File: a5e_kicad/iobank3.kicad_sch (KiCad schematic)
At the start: 3 parts, among them U7 A5EB013B-B23B

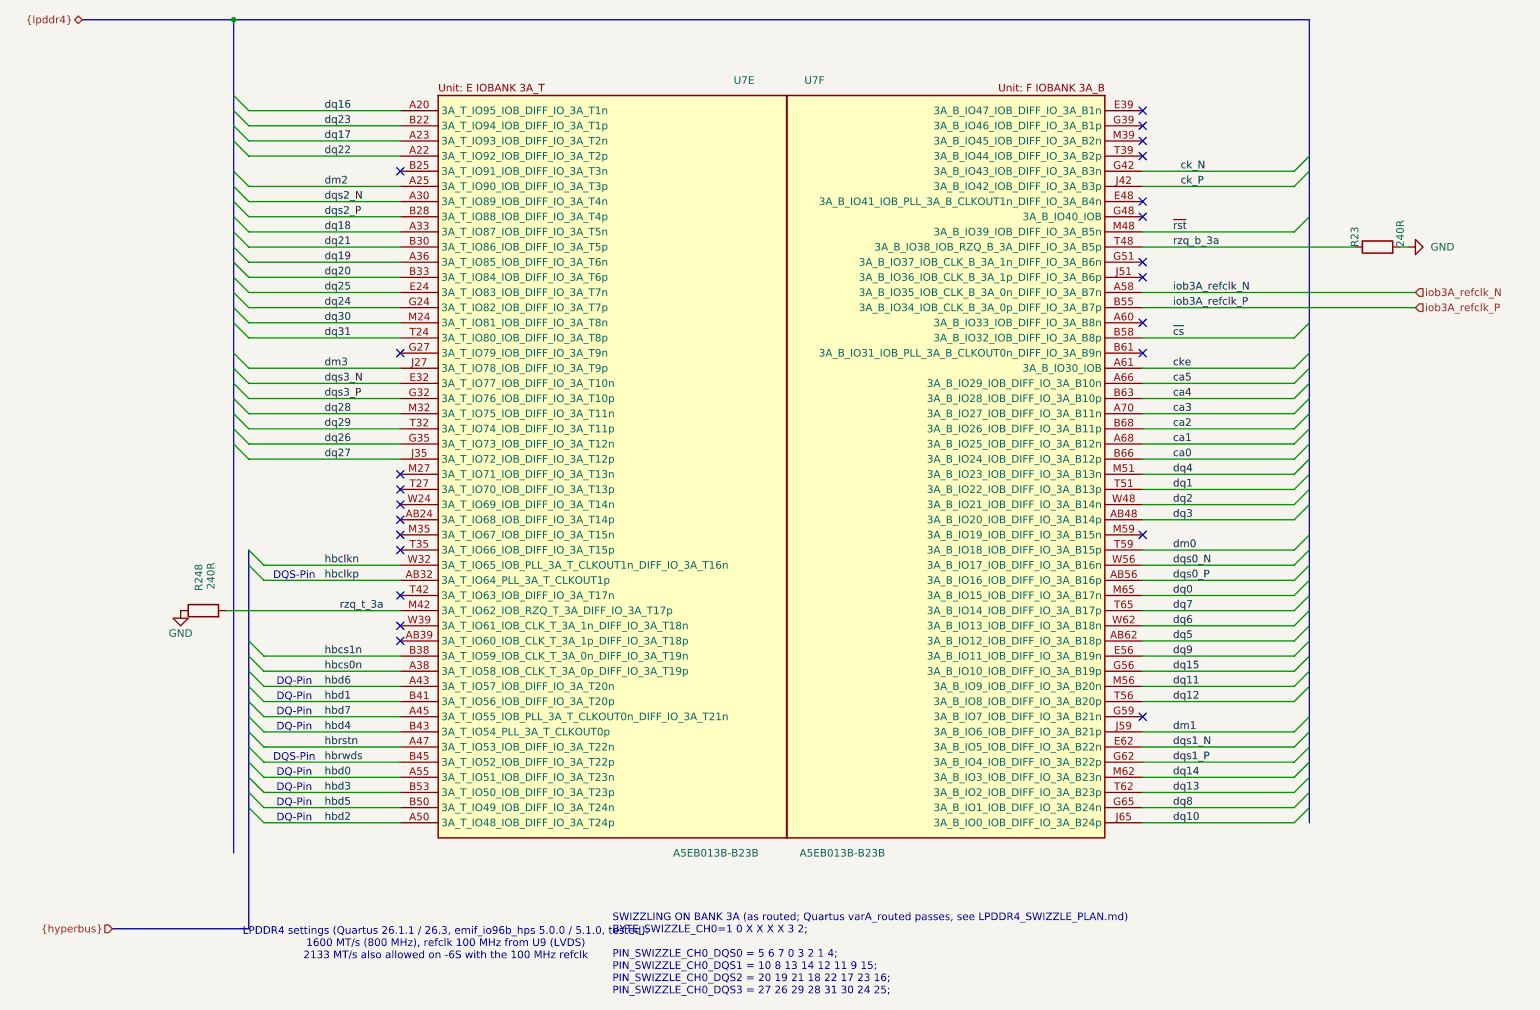
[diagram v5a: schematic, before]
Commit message: Schematic reorg step 7: no global labels, NC flags on unused U7 pins
- hps_uart0_tx/rx, eth_rst_n, phy_rst_n, fpga_led: global labels replaced by
  sheet pins; eth_led_g_n is a local label
- HyperBus labels/bus, the HPS {hps_i2c} bus and the pwr_scl/pwr_sda wiring
  removed (nothing behind them)
- 118 U7 pins that only had a net label: label, stub and bus entry removed,
  no-connect flag added
- Bank 3A notes restacked
- PCB: 124 nets renamed (118 to unconnected-(U7...))

Netdiff: 124 renamed, 0 connectivity diffs. ERC 148 -> 21. DRC parity 0.
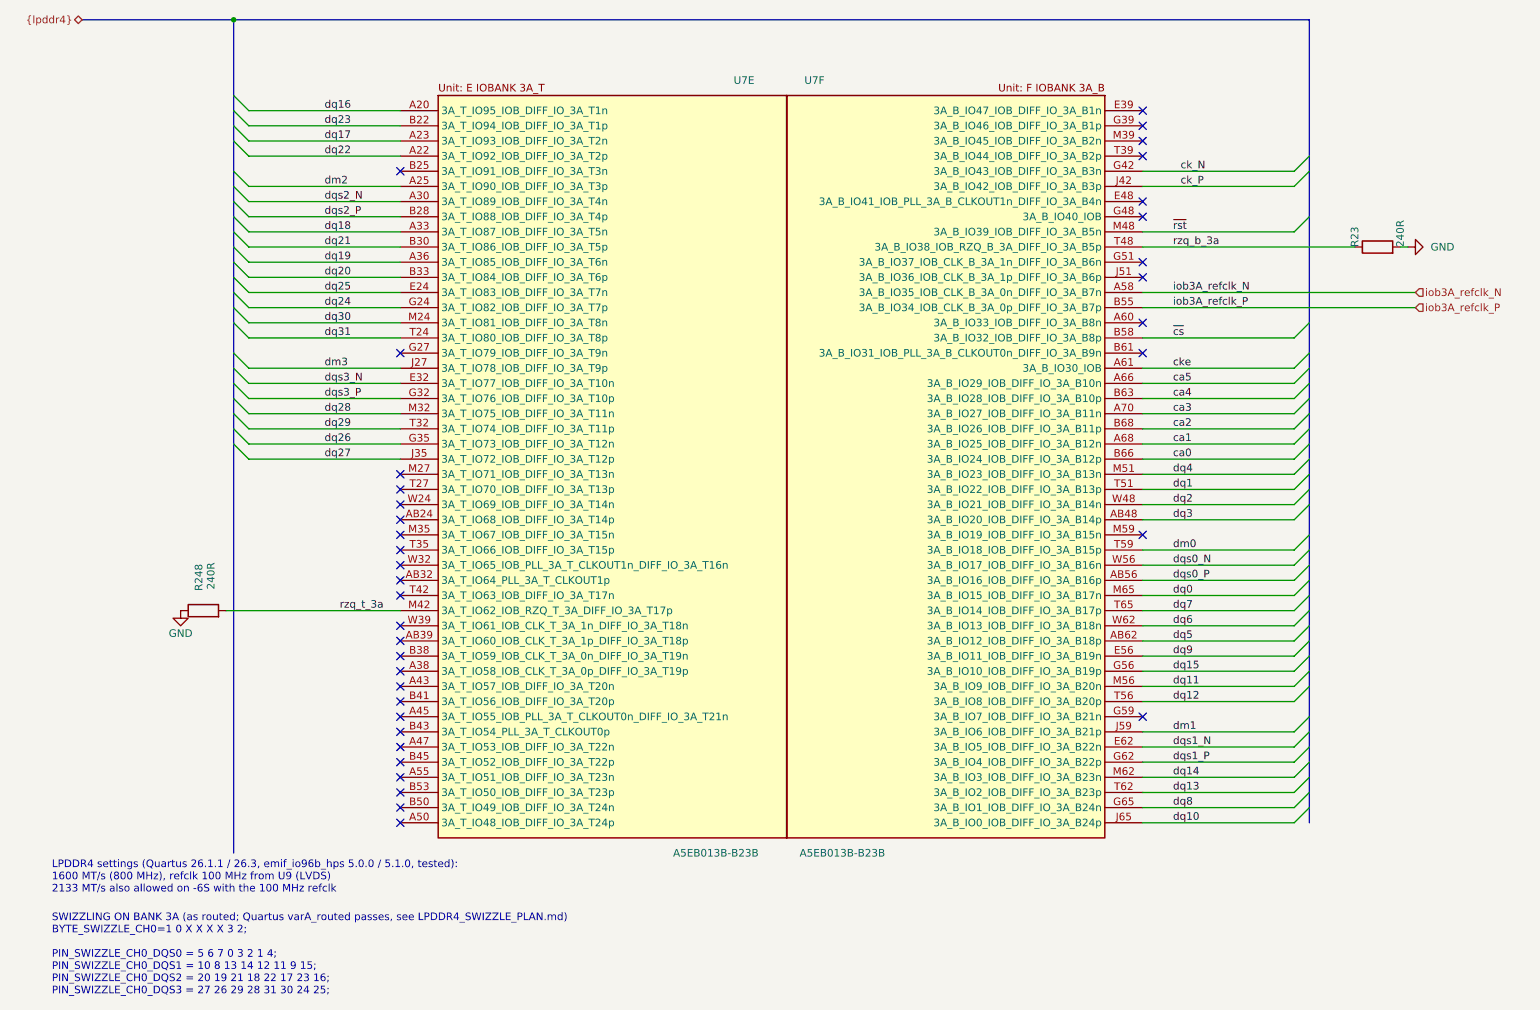
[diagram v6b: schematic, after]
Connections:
- net hbclkn: no longer names the net of U7.W32 (3A_T_IO65_IOB_PLL_3A_T_CLKOUT1n_DIFF_IO_3A_T16n)
- net hbclkp: no longer names the net of U7.AB32 (3A_T_IO64_IOB)
- net hbcs0n: no longer names the net of U7.A38 (3A_T_IO58_IOB_CLK_T_3A_0p_DIFF_IO_3A_T19p)
- net hbcs1n: no longer names the net of U7.B38 (3A_T_IO59_IOB_CLK_T_3A_0n_DIFF_IO_3A_T19n)
- net hbd0: no longer names the net of U7.A55 (3A_T_IO51_IOB_DIFF_IO_3A_T23n)
- net hbd1: no longer names the net of U7.B41 (3A_T_IO56_IOB_DIFF_IO_3A_T20p)
- net hbd2: no longer names the net of U7.A50 (3A_T_IO48_IOB_DIFF_IO_3A_T24p)
- net hbd3: no longer names the net of U7.B53 (3A_T_IO50_IOB_DIFF_IO_3A_T23p)
- net hbd4: no longer names the net of U7.B43 (3A_T_IO54_IOB)
- net hbd5: no longer names the net of U7.B50 (3A_T_IO49_IOB_DIFF_IO_3A_T24n)
- net hbd6: no longer names the net of U7.A43 (3A_T_IO57_IOB_DIFF_IO_3A_T20n)
- net hbd7: no longer names the net of U7.A45 (3A_T_IO55_IOB_PLL_3A_T_CLKOUT0n_DIFF_IO_3A_T21n)
- net hbrstn: no longer names the net of U7.A47 (3A_T_IO53_IOB_DIFF_IO_3A_T22n)
- net hbrwds: no longer names the net of U7.B45 (3A_T_IO52_IOB_DIFF_IO_3A_T22p)
- no-connect marks 23 -> 37
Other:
- note removed: "DQ-Pin"
- note removed: "DQS-Pin"
